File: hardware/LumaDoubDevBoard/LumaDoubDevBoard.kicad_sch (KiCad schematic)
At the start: 135 parts, among them J1 Conn_02x12_Counter_Clockwise, P1 VGA_Male, SW1 CVBS IN, SW10 CVBS/YC OUT, SW11 Free Run, SW12 GP1, SW13 GP2, SW14 GP3, SW15 GP4, SW16 GP5, SW17 GP5, SW18 GP5, SW19 GP5, SW2 YC IN, SW20 GP5, SW3 SoG, SoL, SW4 GP5, SW5 I2P, SW6 Vaseline, SW7 Force 240p, SW8 Notch FIlter, SW9 YPbPr OUT, U1 ADV7280xCP, U2 ADV7390BCPZ, U3 Pico, U4 DEBUG, Y1 ABM8AIG-28.63636MHZ-12-2Z-T3

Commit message: Saved the schematic
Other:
- note added: "PSU Recommended Specs DVDDIO = 3.3v, 20ma DVDD = 1.8v, 110ma AVDD = 1.8v, 100ma PVDD = 1.8v, 20ma .48w Total"
- note added: "PSU Recommended Specs VDD = 1.8v, 68ma 101max VDD_IO = 3.3v, 1ma 10max AVDD = 1.8v, 100ma PVDD = 1.8v, 20ma .48w Total"
- note removed: "Connected to Pico"
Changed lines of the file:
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@@
     (effects (font (size 1.7 1.7)) (justify left bottom))
   )
-  (text "Connected to Pico" (at 132.0546 188.468 0)
+  (text "PSU Recommended Specs\nDVDDIO	= 3.3v, 20ma\nDVDD 	= 1.8v, 110ma\nAVDD	= 1.8v, 100ma\nPVDD	= 1.8v, 20ma\n		  .48w Total"
+    (at 43.0022 58.674 0)
     (effects (font (size 1.27 1.27)) (justify left bottom))
   )
+  (text "PSU Recommended Specs\nVDD		= 1.8v, 68ma	101max \nVDD_IO 	= 3.3v, 1ma		 10max\nAVDD	= 1.8v, 100ma\nPVDD	= 1.8v, 20ma\n		  .48w Total"
+    (at 255.3208 45.3898 0)
+    (effects (font (size 1.27 1.27)) (justify left bottom))
+  )

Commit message: Added to the Schematic, Started PCB Layout
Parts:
- removed D1, D2, D3, D4, D5, D6, D7, D8: LED, symbol Device:LED
- removed JP13, JP14, JP15, JP16, JP17, JP18, JP19, JP20: IN1, symbol Jumper:Jumper_2_Open
- removed R27, R28, R29, R30, R31, R32, R6, R7: R, symbol Device:R
- removed SW1: CVBS IN, symbol Switch:SW_SPST
- removed SW10: CVBS/YC OUT, symbol Switch:SW_SPST
- removed SW11: Free Run, symbol Switch:SW_SPST
- removed SW12: GP1, symbol Switch:SW_SPST
- removed SW13: GP2, symbol Switch:SW_SPST
- removed SW14: GP3, symbol Switch:SW_SPST
- removed SW15: GP4, symbol Switch:SW_SPST
- removed SW16, SW17, SW18, SW19, SW20, SW4: GP5, symbol Switch:SW_SPST
- removed SW2: YC IN, symbol Switch:SW_SPST
- removed SW3: SoG, SoL, symbol Switch:SW_SPST
- removed SW5: I2P, symbol Switch:SW_SPST
- removed SW6: Vaseline, symbol Switch:SW_SPST
- removed SW7: Force 240p, symbol Switch:SW_SPST
- removed SW8: Notch FIlter, symbol Switch:SW_SPST
- removed SW9: YPbPr OUT, symbol Switch:SW_SPST
- added D10, D11, D12, D13, D14, D15, D16, D9: LED, LED_THT:LED_D5.0mm, symbol Device:LED
- added JP23, JP24, JP25, JP26, JP27, JP28, JP29, JP30: IN1, Jumper:SolderJumper-2_P1.3mm_Open_TrianglePad1.0x1.5mm, symbol Jumper:Jumper_2_Open
- added R33, R34, R35, R36, R37, R38, R39, R40: R, Resistor_SMD:R_0603_1608Metric, symbol Device:R
- added S1, S10, S11, S12, S13, S14, S15, S16, S2, S3, S4, S5, S6, S7, S8, S9: SS12D07VG4, EveryThingGoesHere:SW_SS12D07VG4, symbol SS12D07VG4:SS12D07VG4
- C1, C10, C11, C12, C13, C14, C15, C16, C17, C18, C19, C2, C20, C21, C22, C23, C24, C25, C26, C27, C28, C29, C3, C30, C4, C48, C5, C6, C7, C8, C9: footprint (none) -> AAAAAA2:Cap_SMD_0603
- J1: footprint (none) -> Connector_PinHeader_2.54mm:PinHeader_2x12_P2.54mm_Vertical
- JP1, JP10, JP11, JP12, JP2, JP21, JP22, JP3, JP4, JP5, JP6, JP7, JP8, JP9: footprint (none) -> Jumper:SolderJumper-2_P1.3mm_Open_TrianglePad1.0x1.5mm
- R1, R10, R11, R12, R13, R14, R15, R16, R17, R18, R19, R2, R20, R21, R22, R23, R24, R25, R26, R3, R4, R5, R8, R9: footprint (none) -> Resistor_SMD:R_0603_1608Metric
- RN1, RN2: footprint (none) -> Resistor_SMD:R_Array_Convex_4x1206
- TP1, TP10, TP11, TP12, TP2, TP3, TP4, TP5, TP6, TP7, TP8, TP9: footprint (none) -> Connector_PinHeader_2.54mm:PinHeader_1x01_P2.54mm_Vertical
- U3, U4: footprint RPi_Pico:RPi_Pico_SMD_TH -> CAD:RPi_Pico_SMD_TH
- Y1: footprint ABM8AIG25000MHZ122ZT3 -> Library Loader:ABM8AIG25000MHZ122ZT3
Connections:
- net B2 / EX0: now also JP24.2 (B), S10.1
- net B3 / EX1: now also JP25.2 (B), S11.1
- net B4: now also JP26.2 (B), S12.1
- net B5: now also JP28.2 (B), S14.1
- net B6: now also JP29.2 (B), S15.1
- net B7: now also JP30.2 (B), S16.1
- net CVBS IN: now also S1.1
- net CVBS/YC OUT: now also S4.1
- net Force 240p: now also S8.1
- net Free Run / B1: now also JP27.2 (B), S13.1
- net GND: now also D10.1 (K), D11.1 (K), D12.1 (K), D13.1 (K), D14.1 (K), D15.1 (K), D16.1 (K), D9.1 (K), S1.2, S1.S1 (SHIELD), S1.S2 (SHIELD), S10.2, S10.S1 (SHIELD), S10.S2 (SHIELD), S11.2, S11.S1 (SHIELD), S11.S2 (SHIELD), S12.2, S12.S1 (SHIELD), S12.S2 (SHIELD), S13.2, S13.S1 (SHIELD), S13.S2 (SHIELD), S14.2, S14.S1 (SHIELD), S14.S2 (SHIELD), S15.2, S15.S1 (SHIELD), S15.S2 (SHIELD), S16.2, S16.S1 (SHIELD), S16.S2 (SHIELD), S2.2, S2.S1 (SHIELD), S2.S2 (SHIELD), S3.2, S3.S1 (SHIELD), S3.S2 (SHIELD), S4.2, S4.S1 (SHIELD), S4.S2 (SHIELD), S5.2, S5.S1 (SHIELD), S5.S2 (SHIELD), S6.2, S6.S1 (SHIELD), S6.S2 (SHIELD), S7.2, S7.S1 (SHIELD), S7.S2 (SHIELD), S8.2, S8.S1 (SHIELD), S8.S2 (SHIELD), S9.2, S9.S1 (SHIELD), S9.S2 (SHIELD)
- net Line Double: now also S5.1
- net Notch Filter: now also S7.1
- net SoG / B0: now also JP23.2 (B), S9.1
- net Vaseline: now also S6.1
- net YC IN: now also S2.1
- net YPbPr OUT: now also S3.1
- new net: D13.2 (A), R37.1
- new net: JP27.1 (A), R37.2
- new net: D9.2 (A), R33.1
- new net: D10.2 (A), R34.1
- new net: JP24.1 (A), R34.2
- new net: JP25.1 (A), R35.2
- new net: D15.2 (A), R39.1
- new net: JP29.1 (A), R39.2
- new net: D11.2 (A), R35.1
- new net: JP30.1 (A), R40.2
- new net: D14.2 (A), R38.1
- new net: JP28.1 (A), R38.2
- new net: JP23.1 (A), R33.2
- new net: D12.2 (A), R36.1
- new net: JP26.1 (A), R36.2
- new net: D16.2 (A), R40.1

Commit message: Add power management to schematic
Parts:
- added C31, C32: 10μF, Capacitor_SMD:C_0603_1608Metric, symbol Device:C_Small
- added C33, C34, C36, C37, C39, C40: 22μF, Capacitor_SMD:C_0603_1608Metric, symbol Device:C_Small
- added C35, C38: 0.1μF, Capacitor_SMD:C_0402_1005Metric, symbol Device:C_Small
- added C41, C42, C43, C44, C45, C46, C47, C49, C50, C51: 1μF, Capacitor_SMD:C_0402_1005Metric, symbol Device:C_Small
- added F1, F2: SMD0805B050TF, Fuse:Fuse_0805_2012Metric, symbol Device:Polyfuse
- added IC1: TPS2116DRLR, SOTFL50P160X60-8N, symbol SamacSys_Parts:TPS2116DRLR
- added IC2: TPS62A01ADRLR, SOTFL50P160X60-6N, symbol SamacSys_Parts:TPS62A01ADRLR
- added J2: 217179-0001, shinobi:2171790001_MOL_650876, symbol Connector:USB_C_Receptacle_USB2.0_16P
- added J3: Conn_01x02_Pin, Connector_PinHeader_2.54mm:PinHeader_1x02_P2.54mm_Vertical, symbol Connector:Conn_01x02_Pin
- added L1, L2: DFE252012P-1R0M=P2, Inductor_SMD:L_1008_2520Metric, symbol Device:L
- added R27: 15k, Resistor_SMD:R_0402_1005Metric, symbol Device:R_Small
- added R28, R6, R7: 5.1k, Resistor_SMD:R_0402_1005Metric, symbol Device:R_Small
- added R29: 511k, Resistor_SMD:R_0402_1005Metric, symbol Device:R_Small
- added R30: 91k, Resistor_SMD:R_0402_1005Metric, symbol Device:R_Small
- added R31, R42, R43, R44, R45, R46, R47: LVK12R100CER, Resistor_SMD:R_Shunt_Ohmite_LVK12, symbol Device:R_Shunt
- added R32: 215k, Resistor_SMD:R_0402_1005Metric, symbol Device:R_Small
- added R41: 100k, Resistor_SMD:R_0402_1005Metric, symbol Device:R_Small
- added TP13, TP14, TP15, TP16, TP17, TP18, TP19, TP20, TP21, TP22, TP23, TP24, TP25, TP26: TestPoint, TestPoint:TestPoint_THTPad_D1.5mm_Drill0.7mm, symbol Connector:TestPoint
- added U10, U6, U7, U8, U9: LP5907MFX-1.8, Package_TO_SOT_SMD:SOT-23-5, symbol Regulator_Linear:LP5907MFX-1.8
- added U5: TPS631000DRLR, SOTFL50P160X60-8N, symbol SamacSys_Parts:TPS631000DRLR
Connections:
- net +3V3: now also R29.1, R31.1; no longer C28.2, C29.2, C30.2, C48.1, U2.19 (V_{AA})
- net GND: now also C31.2, C32.2, C33.2, C34.2, C35.2, C36.2, C37.2, C38.2, C39.2, C40.2, C41.2, C42.2, C43.2, C44.2, C45.2, C46.2, C47.2, C49.2, C50.2, C51.2, IC1.1 (GND), IC2.1 (GND), J2.1 (GND), J2.13 (GND), J2.14 (GND), J2.15 (GND), J2.16 (GND), J2.2 (GND), J2.3 (GND), J2.4 (GND), J2.A1/B12 (GND_2), J2.B1/A12 (GND), J2.S_1_H1 (GND), J2.S_1_H2 (GND), J2.S_2_H1 (GND), J2.S_2_H2 (GND), J2.S_3_H1 (GND), J2.S_3_H2 (GND), J2.S_4_H1 (GND), J2.S_4_H2 (GND), J3.2 (Pin_2), R28.2, R30.2, R41.2, R6.2, R7.2, U10.2 (GND), U5.6 (MODE), U5.7 (GND), U6.2 (GND), U7.2 (GND), U8.2 (GND), U9.2 (GND)
- removed net +1V8: C10.2, C12.1, C15.1, C20.1, C21.1, C22.1, C23.1, C26.2, C27.2, C3.1, C4.1, C5.1, C6.1, C7.2, C8.2, C9.2, J1.2 (Pin_2), U1.13 (DVDD), U1.16 (PVDD), U1.21 (AVDD), U1.3 (DVDD), U2.17 (P_{VDD}), U2.28 (V_{DD}), U2.5 (V_{DD})
- net +5V renamed VMUX
- net VMUX: now also C36.1, C37.1, IC1.2 (VOUT), IC1.7 (VOUT_2), IC2.3 (VIN), IC2.4 (EN), U5.4 (VIN), U5.5 (EN)
- new net: C42.1, R43.4, U6.5 (OUT)
- new net: IC1.4 (PR1), R27.2, R28.1
- new net: R43.3, TP17.1
- new net: F1.2, IC1.3 (VIN1), IC1.5 (MODE), R27.1
- new net: IC2.2 (SW), L2.1
- new net: C38.1, C39.1, C40.1, L2.2, R42.4
- new net: R44.3, TP19.1
- new net: R43.2, TP18.1
- new net: R45.3, TP21.1
- new net: R42.2, TP16.1
- new net: R42.3, TP15.1
- new net: IC2.5 (FB), R32.2, R41.1
- new net: C33.1, C34.1, C35.1, R31.4, U5.1 (VOUT)
- new net: C46.1, R45.4, U8.5 (OUT)
- new net: C51.1, R47.4, U10.5 (OUT)
- new net: R29.2, R30.1, U5.8 (FB)
- new net: F2.2, IC1.6 (VIN2)
- new net: R31.2, TP14.1
- new net: R31.3, TP13.1
- new net: R44.2, TP20.1
- new net: L1.1, U5.3 (LX1)
- new net: L1.2, U5.2 (LX2)
- new net: C49.1, R46.4, U9.5 (OUT)
- new net: C44.1, R44.4, U7.5 (OUT)
- new net: J2.A5 (CC1), R7.1
- new net: J2.B5 (CC2), R6.1
- new net: R45.2, TP22.1
- new net: R47.2, TP26.1
- new net: R47.3, TP25.1
- new net: R46.3, TP23.1
- new net: R46.2, TP24.1
- new net +1V89: C41.1, C43.1, C45.1, C47.1, C50.1, J1.2 (Pin_2), R32.1, R42.1, U10.1 (IN), U10.3 (EN), U6.1 (IN), U6.3 (EN), U7.1 (IN), U7.3 (EN), U8.1 (IN), U8.3 (EN), U9.1 (IN), U9.3 (EN)
- new net ADV7280_AVDD: C10.2, C9.2, R46.1, U1.21 (AVDD)
- new net ADV7280_DVDD: C3.1, C4.1, C5.1, C6.1, R43.1, U1.13 (DVDD), U1.3 (DVDD)
- new net ADV7390_AVDD: C28.2, C29.2, C30.2, C48.1, R47.1, U2.19 (V_{AA})
- new net ADV7390_DVDD: C20.1, C21.1, C22.1, C23.1, R44.1, U2.28 (V_{DD}), U2.5 (V_{DD})
- new net PVDD: C12.1, C15.1, C26.2, C27.2, C7.2, C8.2, R45.1, U1.16 (PVDD), U2.17 (P_{VDD})
- new net VBAT: C32.1, F2.1, J3.1 (Pin_1)
- new net VBUS: C31.1, F1.1, J2.A4/B9 (VBUS), J2.B4/A9 (VBUS)
- no-connect marks 0 -> 8
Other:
- note added: "1.89V buck"
- note added: "1.8V LDOs"
- note added: "169 is a standard value resistor that you can buy. 170 is not"
- note added: "3.3V buck-boost"
- note added: "Current sense I = V x 0.1"
- note added: "Muxed power output (USB or battery) USB has priority"
- note added: "Not sure which rail you want to break out here"
- note added: "PSU or 1S li-ion input 3V - 5.5V!"
- note added: "Part operates in auto PSM for better efficiency at low current"
- note added: "Part operates in forced-PWM mode (low ripple)"
- note added: "Power Inputs"
- moved on the sheet: C1, C10, C11, C12, C13, C14, C15, C16, C17, C18, C19, C2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

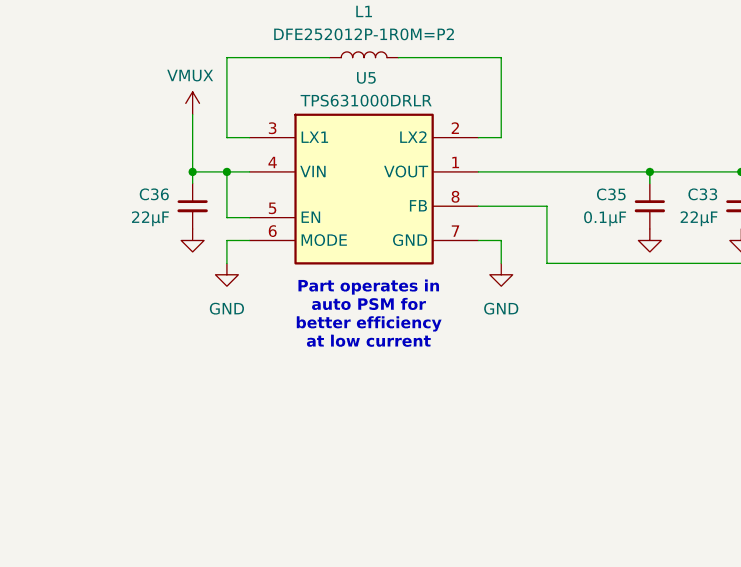
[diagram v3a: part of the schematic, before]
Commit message: Update 3.3v buck-boost to FPWM mode
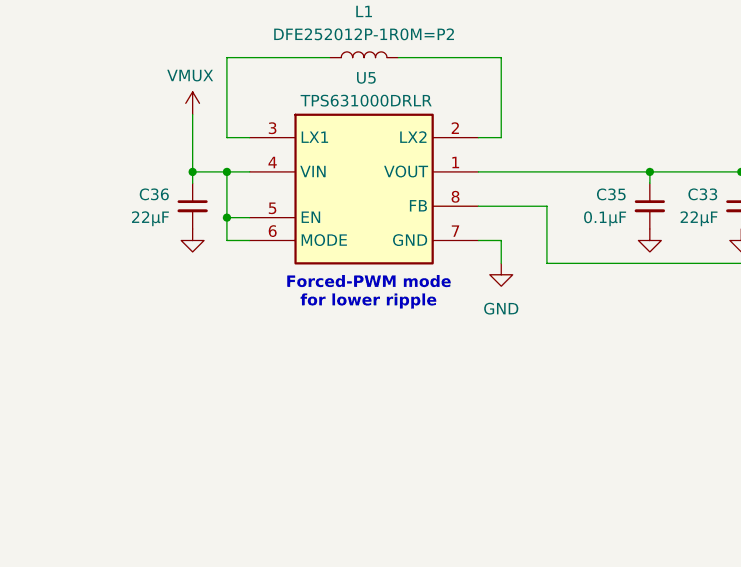
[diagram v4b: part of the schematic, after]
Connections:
- net GND: no longer U5.6 (MODE)
- net VMUX: now also U5.6 (MODE)
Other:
- note added: "Forced-PWM mode for lower ripple"
- note removed: "Part operates in auto PSM for better efficiency at low current"
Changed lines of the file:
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@@
 		)
 	)
-	(text "Part operates in\nauto PSM for\nbetter efficiency\nat low current"
+	(text "Forced-PWM mode\nfor lower ripple"
 		(exclude_from_sim no)
-		(at 86.868 482.092 0)
+		(at 86.868 479.552 0)
 		(effects
 			(font
@@
 	)
 	(junction
+		(at 71.12 471.17)
+		(diameter 0)
+		(color 0 0 0 0)
+	)
+	(junction
 		(at 187.96 467.36)
 		(diameter 0)
@@
 	(wire
 		(pts
+			(xy 71.12 473.71) (xy 71.12 471.17)
+		)
+		(stroke
+			(width 0)
+			(type default)
+		)
+	)
+	(wire
+		(pts
 			(xy 306.07 544.83) (xy 308.61 544.83)
 		)
@@
 	(wire
 		(pts
-			(xy 73.66 473.71) (xy 71.12 473.71)
-		)
-		(stroke
-			(width 0)
-			(type default)
-		)
-	)
-	(wire
-		(pts
 			(xy 84.9376 123.063) (xy 79.8576 123.063)
 		)
@@
 	(wire
 		(pts
-			(xy 71.12 473.71) (xy 71.12 476.25)
-		)
-		(stroke
-			(width 0)
-			(type default)
-		)
-	)
-	(wire
-		(pts
 			(xy 370.84 69.85) (xy 393.7 69.85)
 		)
@@
 	(wire
 		(pts
+			(xy 73.66 473.71) (xy 71.12 473.71)
+		)
+		(stroke
+			(width 0)
+			(type default)
+		)
+	)
+	(wire
+		(pts
 			(xy 448.437 330.0476) (xy 451.0024 330.0476)
 		)
@@
 					(unit 1)
 				)
-			)
-		)
-	)
-	(symbol
-		(lib_id "power:GND")
-		(at 71.12 476.25 0)
-		(unit 1)
-		(exclude_from_sim no)
-		(in_bom yes)
-		(on_board yes)
-		(dnp no)
-		(fields_autoplaced yes)
-		(property "Reference" "#PWR0116"
-			(at 71.12 482.6 0)
-			(effects
-				(font
-					(size 1.27 1.27)
-				)
-				(hide yes)
-			)
-		)
-		(property "Value" "GND"
-			(at 71.12 481.33 0)
-			(effects
-				(font
-					(size 1.27 1.27)
-				)
-			)
-		)
-		(property "Footprint" ""
-			(at 71.12 476.25 0)
-			(effects
-				(font
-					(size 1.27 1.27)
-				)
-				(hide yes)
-			)
-		)
-		(property "Datasheet" ""
-			(at 71.12 476.25 0)
-			(effects
-				(font
-					(size 1.27 1.27)
-				)
-				(hide yes)
-			)
-		)
-		(property "Description" "Power symbol creates a global label with name \"GND\" , ground"
-			(at 71.12 476.25 0)
-			(effects
-				(font
-					(size 1.27 1.27)
-				)
-				(hide yes)
-			)
-		)
-		(pin "1"
-		)
-		(instances
-			(project "LumaDoubDevBoard"
-				(path "/22b97ae5-fe59-4d93-94b6-97d72fa5acf6"
-					(reference "#PWR0116")
-					(unit 1)
-				)

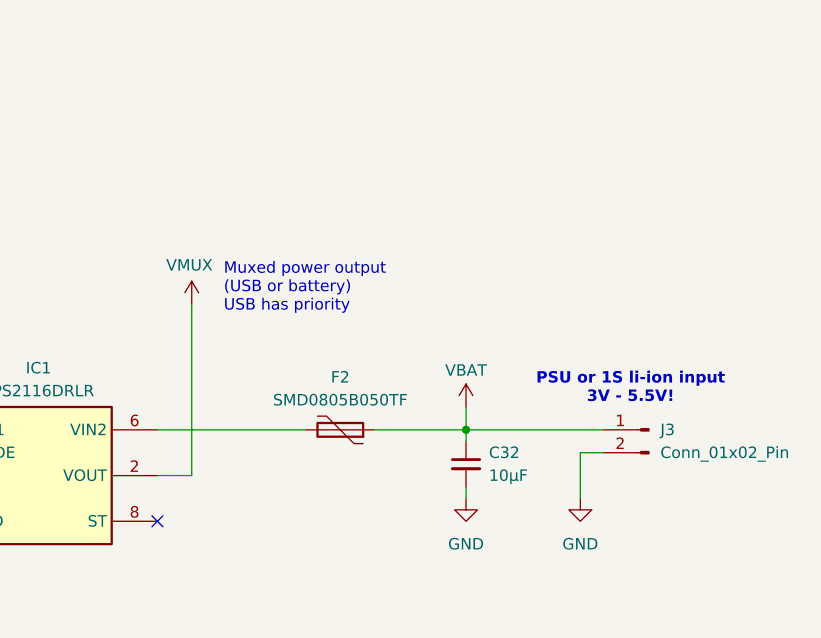
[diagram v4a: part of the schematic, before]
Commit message: Add current-sense to VMUX
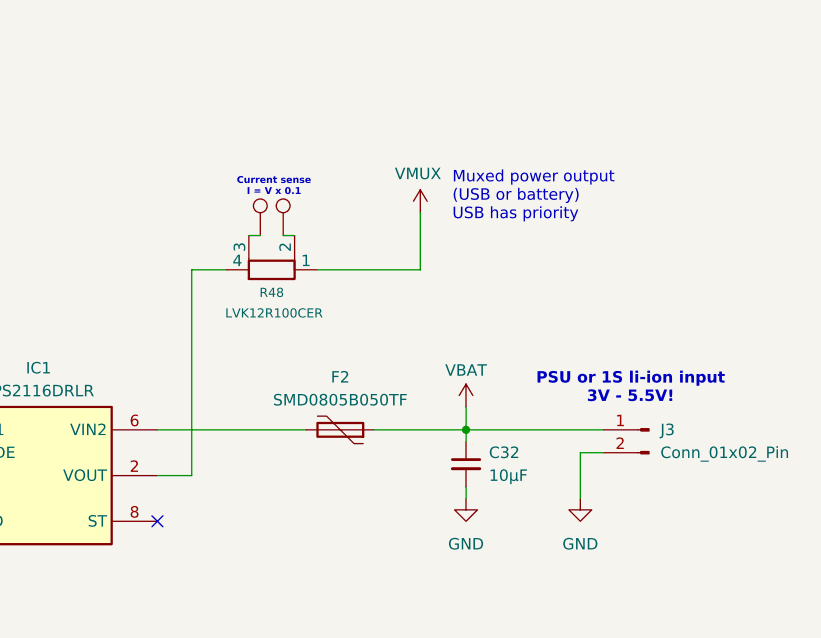
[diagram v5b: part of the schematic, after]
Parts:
- added R48: LVK12R100CER, Resistor_SMD:R_Shunt_Ohmite_LVK12, symbol Device:R_Shunt
- added TP27, TP28: TestPoint, TestPoint:TestPoint_THTPad_D1.5mm_Drill0.7mm, symbol Connector:TestPoint
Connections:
- net VMUX: now also R48.1; no longer IC1.2 (VOUT), IC1.7 (VOUT_2)
- new net: R48.2, TP28.1
- new net: IC1.2 (VOUT), IC1.7 (VOUT_2), R48.4
- new net: R48.3, TP27.1

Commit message: Restore WIP layout file
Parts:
- IC1, U5: footprint SOTFL50P160X60-8N -> SamacSys_Parts:SOTFL50P160X60-8N
- IC2: footprint SOTFL50P160X60-6N -> SamacSys_Parts:SOTFL50P160X60-6N
- J2: footprint shinobi:2171790001_MOL_650876 -> SamacSys_Parts:2171790001
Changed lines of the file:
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@@
 			)
 		)
-		(property "Footprint" "SOTFL50P160X60-8N"
+		(property "Footprint" "SamacSys_Parts:SOTFL50P160X60-8N"
 			(at 175.26 478.46 0)
 			(effects
@@
 			)
 		)
-		(property "Footprint" "shinobi:2171790001_MOL_650876"
+		(property "Footprint" "SamacSys_Parts:2171790001"
 			(at 80.01 398.78 0)
 			(effects
@@
 			)
 		)
-		(property "Footprint" "SOTFL50P160X60-6N"
+		(property "Footprint" "SamacSys_Parts:SOTFL50P160X60-6N"
 			(at 212.09 562.28 0)
 			(effects
@@
 			)
 		)
-		(property "Footprint" "SOTFL50P160X60-8N"
+		(property "Footprint" "SamacSys_Parts:SOTFL50P160X60-8N"
 			(at 97.79 557.2 0)
 			(effects
